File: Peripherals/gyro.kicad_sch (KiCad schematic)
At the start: 6 parts, among them U4 I3G4250D

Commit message: Reorganised repo
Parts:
- C14: value 470n -> (none); footprint Capacitor_SMD:C_0603_1608Metric -> (none)
- C15: value 10n -> (none); footprint Capacitor_SMD:C_0603_1608Metric -> (none)
- C16: value 10uF -> (none); footprint Capacitor_SMD:C_0603_1608Metric -> (none)
- C17: value 100nF -> (none); footprint Capacitor_SMD:C_0603_1608Metric -> (none)
- R10: value 10k -> (none); footprint Resistor_SMD:R_0603_1608Metric -> (none)
- U4: value I3G4250D -> (none); footprint YAR_Sensors:I3G4250D -> (none)
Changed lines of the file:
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@@
   (symbol (lib_id "power:GND") (at 76.2 83.82 0) (unit 1)
     (in_bom yes) (on_board yes) (fields_autoplaced)
-    (property "Reference" "#PWR033" (id 0) (at 76.2 90.17 0)
+    (property "Reference" "#PWR?" (id 0) (at 76.2 90.17 0)
       (effects (font (size 1.27 1.27)) hide)
     )
-    (property "Value" "GND" (id 1) (at 76.2 88.9 0))
+    (property "Value" "" (id 1) (at 76.2 88.9 0))
     (property "Footprint" "" (id 2) (at 76.2 83.82 0)
       (effects (font (size 1.27 1.27)) hide)
@@
       (effects (font (size 1.27 1.27)) (justify left))
     )
-    (property "Value" "100nF" (id 1) (at 147.32 50.8 0)
+    (property "Value" "" (id 1) (at 147.32 50.8 0)
       (effects (font (size 1.27 1.27)) (justify left))
     )
-    (property "Footprint" "Capacitor_SMD:C_0603_1608Metric" (id 2) (at 144.4752 53.34 0)
+    (property "Footprint" "" (id 2) (at 144.4752 53.34 0)
       (effects (font (size 1.27 1.27)) hide)
     )
@@
   (symbol (lib_id "power:GND") (at 76.2 45.72 0) (unit 1)
     (in_bom yes) (on_board yes) (fields_autoplaced)
-    (property "Reference" "#PWR032" (id 0) (at 76.2 52.07 0)
+    (property "Reference" "#PWR?" (id 0) (at 76.2 52.07 0)
       (effects (font (size 1.27 1.27)) hide)
     )
-    (property "Value" "GND" (id 1) (at 76.2 50.8 0))
+    (property "Value" "" (id 1) (at 76.2 50.8 0))
     (property "Footprint" "" (id 2) (at 76.2 45.72 0)
       (effects (font (size 1.27 1.27)) hide)
@@
       (effects (font (size 1.27 1.27)) (justify left))
     )
-    (property "Value" "10uF" (id 1) (at 135.89 50.8 0)
+    (property "Value" "" (id 1) (at 135.89 50.8 0)
       (effects (font (size 1.27 1.27)) (justify left))
     )
-    (property "Footprint" "Capacitor_SMD:C_0603_1608Metric" (id 2) (at 133.0452 53.34 0)
+    (property "Footprint" "" (id 2) (at 133.0452 53.34 0)
       (effects (font (size 1.27 1.27)) hide)
     )
@@
   (symbol (lib_id "power:+3V3") (at 115.57 83.82 180) (unit 1)
     (in_bom yes) (on_board yes) (fields_autoplaced)
-    (property "Reference" "#PWR034" (id 0) (at 115.57 80.01 0)
+    (property "Reference" "#PWR?" (id 0) (at 115.57 80.01 0)
       (effects (font (size 1.27 1.27)) hide)
     )
-    (property "Value" "+3V3" (id 1) (at 115.57 88.9 0))
+    (property "Value" "" (id 1) (at 115.57 88.9 0))
     (property "Footprint" "" (id 2) (at 115.57 83.82 0)
       (effects (font (size 1.27 1.27)) hide)
@@
   (symbol (lib_id "power:+3V3") (at 148.59 40.64 0) (unit 1)
     (in_bom yes) (on_board yes) (fields_autoplaced)
-    (property "Reference" "#PWR036" (id 0) (at 148.59 44.45 0)
+    (property "Reference" "#PWR?" (id 0) (at 148.59 44.45 0)
       (effects (font (size 1.27 1.27)) hide)
     )
-    (property "Value" "+3V3" (id 1) (at 148.59 35.56 0))
+    (property "Value" "" (id 1) (at 148.59 35.56 0))
     (property "Footprint" "" (id 2) (at 148.59 40.64 0)
       (effects (font (size 1.27 1.27)) hide)
@@
       (effects (font (size 1.27 1.27)) (justify right))
     )
-    (property "Value" "470n" (id 1) (at 88.9 50.8 0)
+    (property "Value" "" (id 1) (at 88.9 50.8 0)
       (effects (font (size 1.27 1.27)) (justify right))
     )
-    (property "Footprint" "Capacitor_SMD:C_0603_1608Metric" (id 2) (at 91.44 44.1452 0)
+    (property "Footprint" "" (id 2) (at 91.44 44.1452 0)
       (effects (font (size 1.27 1.27)) hide)
     )
@@
   (symbol (lib_id "power:GND") (at 149.86 55.88 0) (unit 1)
     (in_bom yes) (on_board yes) (fields_autoplaced)
-    (property "Reference" "#PWR037" (id 0) (at 149.86 62.23 0)
+    (property "Reference" "#PWR?" (id 0) (at 149.86 62.23 0)
       (effects (font (size 1.27 1.27)) hide)
     )
-    (property "Value" "GND" (id 1) (at 149.86 60.96 0))
+    (property "Value" "" (id 1) (at 149.86 60.96 0))
     (property "Footprint" "" (id 2) (at 149.86 55.88 0)
       (effects (font (size 1.27 1.27)) hide)
@@
       (effects (font (size 1.27 1.27)) (justify right))
     )
-    (property "Value" "10n" (id 1) (at 93.9799 31.75 0)
+    (property "Value" "" (id 1) (at 93.9799 31.75 0)
       (effects (font (size 1.27 1.27)) (justify right))
     )
-    (property "Footprint" "Capacitor_SMD:C_0603_1608Metric" (id 2) (at 88.9 36.5252 0)
+    (property "Footprint" "" (id 2) (at 88.9 36.5252 0)
       (effects (font (size 1.27 1.27)) hide)
     )
@@
       (effects (font (size 1.27 1.27)) (justify left))
     )
-    (property "Value" "10k" (id 1) (at 83.8199 33.02 0)
+    (property "Value" "" (id 1) (at 83.8199 33.02 0)
       (effects (font (size 1.27 1.27)) (justify left))
     )
-    (property "Footprint" "Resistor_SMD:R_0603_1608Metric" (id 2) (at 82.55 37.338 90)
+    (property "Footprint" "" (id 2) (at 82.55 37.338 90)
       (effects (font (size 1.27 1.27)) hide)
     )
@@
     (in_bom yes) (on_board yes)
     (property "Reference" "U4" (id 0) (at 83.82 55.88 0))
-    (property "Value" "I3G4250D" (id 1) (at 83.82 58.42 0))
-    (property "Footprint" "YAR_Sensors:I3G4250D" (id 2) (at 97.79 46.99 0)
+    (property "Value" "" (id 1) (at 83.82 58.42 0))
+    (property "Footprint" "" (id 2) (at 97.79 46.99 0)
       (effects (font (size 1.27 1.27)) hide)
     )
@@
   (symbol (lib_id "power:GND") (at 121.92 74.93 90) (unit 1)
     (in_bom yes) (on_board yes) (fields_autoplaced)
-    (property "Reference" "#PWR035" (id 0) (at 128.27 74.93 0)
+    (property "Reference" "#PWR?" (id 0) (at 128.27 74.93 0)
       (effects (font (size 1.27 1.27)) hide)
     )
-    (property "Value" "GND" (id 1) (at 125.73 74.9299 90)
+    (property "Value" "" (id 1) (at 125.73 74.9299 90)
       (effects (font (size 1.27 1.27)) (justify right))
     )

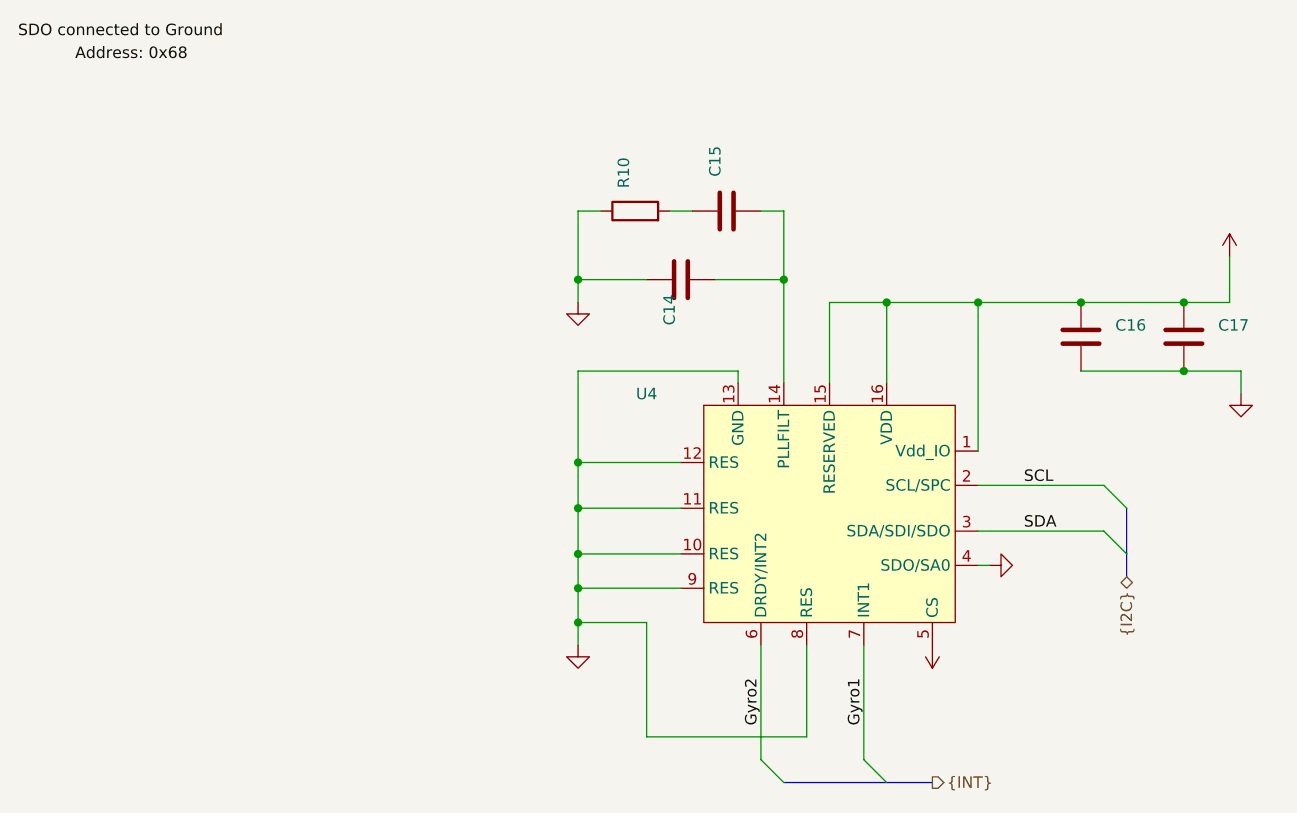
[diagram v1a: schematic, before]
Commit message: rev2 changes excluding pyro
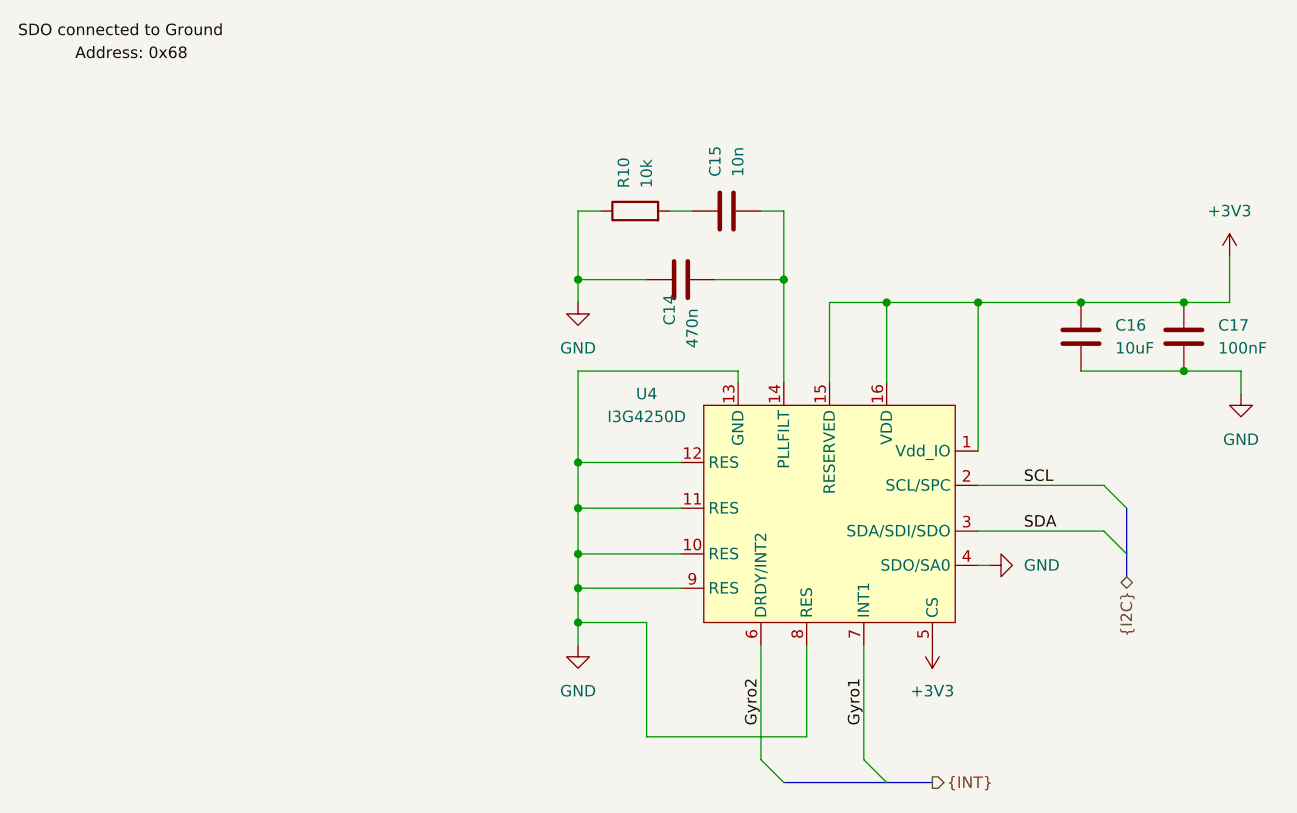
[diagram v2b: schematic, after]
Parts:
- C14: value (none) -> 470n; footprint (none) -> Capacitor_SMD:C_0603_1608Metric
- C15: value (none) -> 10n; footprint (none) -> Capacitor_SMD:C_0603_1608Metric
- C16: value (none) -> 10uF; footprint (none) -> Capacitor_SMD:C_0603_1608Metric
- C17: value (none) -> 100nF; footprint (none) -> Capacitor_SMD:C_0603_1608Metric
- R10: value (none) -> 10k; footprint (none) -> Resistor_SMD:R_0603_1608Metric
- U4: value (none) -> I3G4250D; footprint (none) -> YAR_Sensors:I3G4250D
